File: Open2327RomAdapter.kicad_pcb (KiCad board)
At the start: 2 copper layers, 19.6 x 40.6 mm, 5 parts, among them P1 CONN_01X02, U1 2364, U2 27128

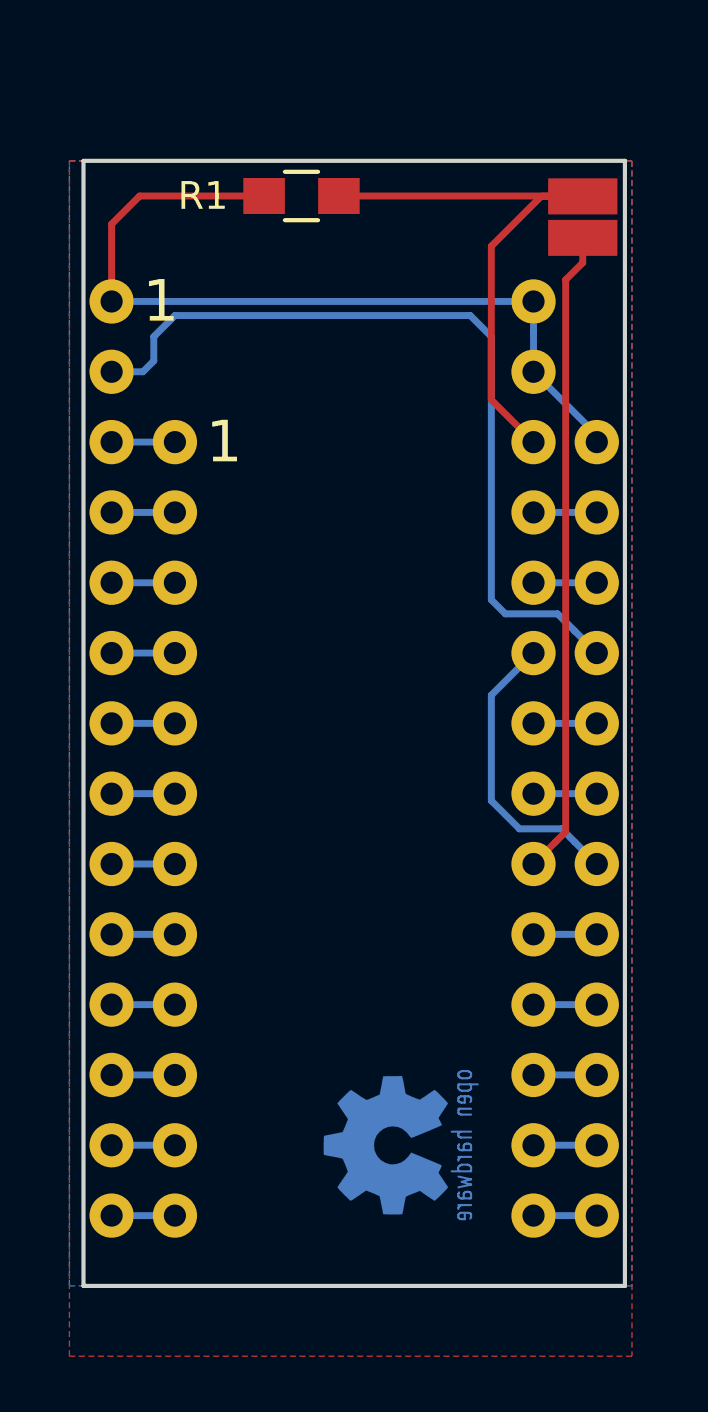
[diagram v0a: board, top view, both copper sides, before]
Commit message: Add pull-up resistors
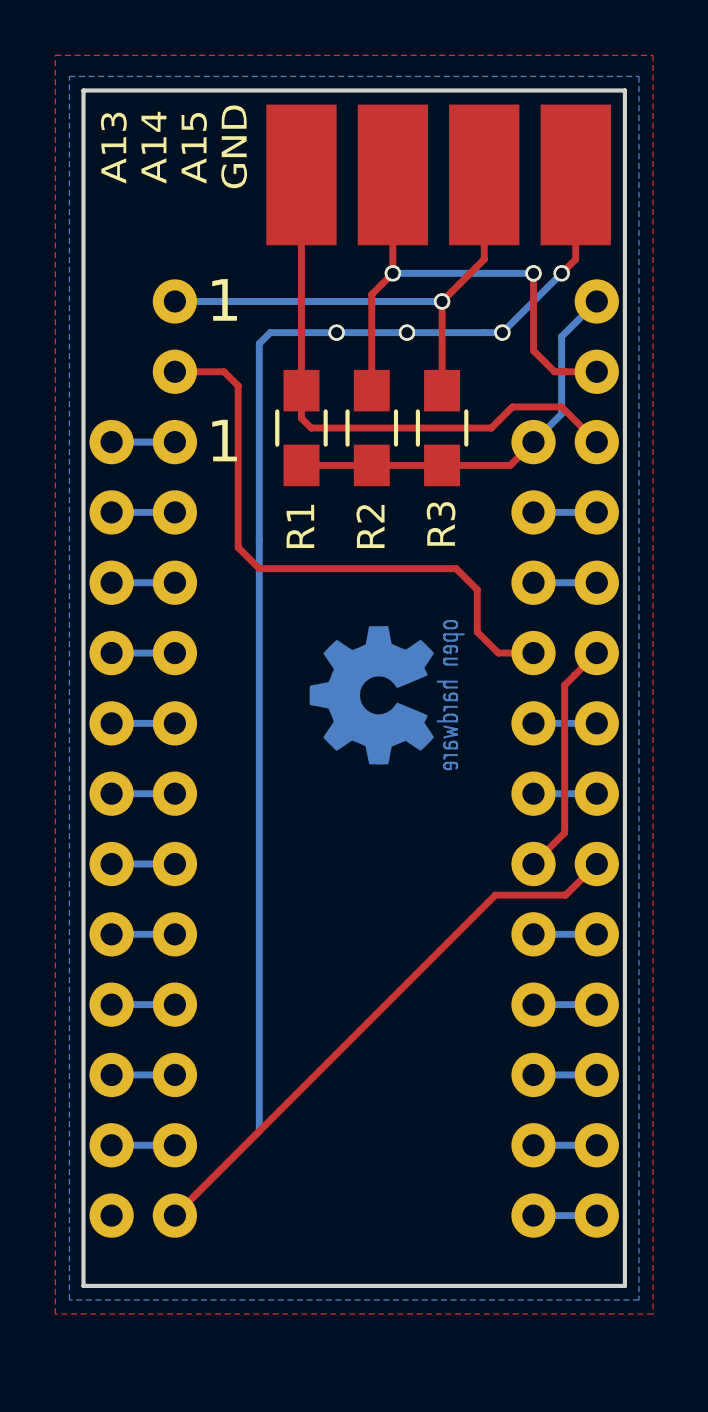
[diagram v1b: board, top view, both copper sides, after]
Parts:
- added R2: 10K, Resistors_SMD:R_0805_HandSoldering, F.Cu at (155.7, 106.2)
- added R3: 10K, Resistors_SMD:R_0805_HandSoldering, F.Cu at (158.2, 106.2)
- P1: value CONN_01X02 -> CONN_01X04; footprint Sukko:LoosePads-2-NoSilkS -> Sukko:LoosePads-4
- moved G*** 16.3 mm to (155.7, 115.8)
- moved R1 8.38 mm to (153.2, 106.2), turned to 270 degrees
- moved P1 5.55 mm to (158.0, 97.0)
- moved U1 2.29 mm to (146.3, 106.7)
- moved U2 2.29 mm to (148.6, 101.6)
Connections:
- R1 pad 1: Net-(P1-Pad2) -> Net-(P1-Pad4)
- U2 pad 1: VCC -> Net-(P1-Pad2)
- U2 pad 26: Net-(P1-Pad2) -> Net-(P1-Pad4)
- U2 pad 27: VCC -> Net-(P1-Pad3)
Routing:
- net GND: track 25.6 -> 69.0 mm, vias 0 -> 4
- net Net-(P1-Pad4): track 0.00 -> 20.4 mm
- net Net-(P1-Pad3): track 0.00 -> 18.6 mm, vias 0 -> 2
- net VCC: track 30.2 -> 14.8 mm
- net Net-(U1-Pad21): track 29.5 -> 21.5 mm
- net Net-(P1-Pad2): track 20.6 -> 18.1 mm, vias 0 -> 1
- net Net-(U1-Pad18): track 10.7 -> 8.57 mm
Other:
- board size 19.6 x 40.6 mm -> 19.6 x 43.2 mm
- board text added: "A13 A14 A15 GND"
- board text added: "https://github.com/SukkoPera/Open2327RomAdapter"
- board text removed: "https://github.com/SukkoPera/"

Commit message: Move pull-up resistors to bottom of board
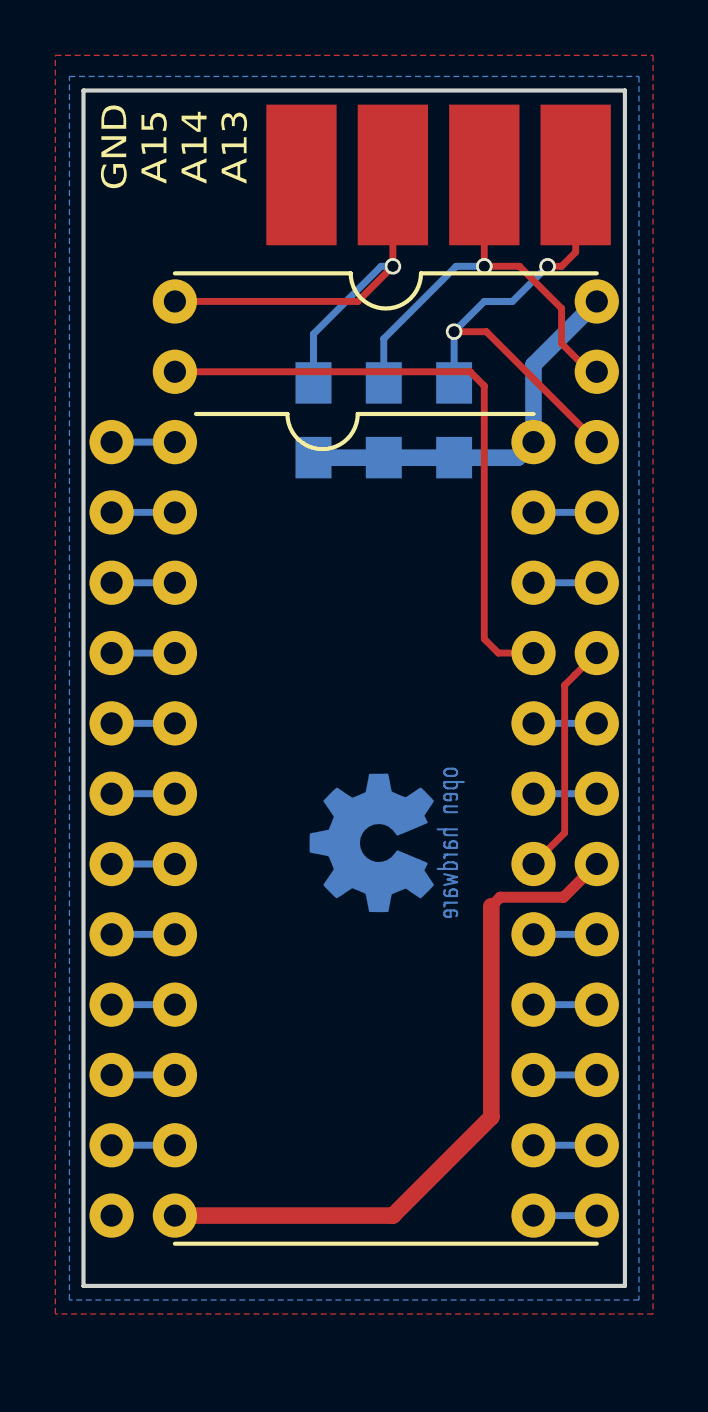
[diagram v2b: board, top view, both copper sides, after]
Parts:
- R1, R2, R3: moved to B.Cu
- U1: footprint Sukko:DIP-24_W15.24mm-NoSilkS -> Sukko:DIP-24_W15.24mm-Notch
- U2: footprint Sukko:DIP-28_W15.24mm-NoSilkS -> Sukko:DIP-28_W15.24mm-Notch
- moved R1 5.52 mm to (158.7, 105.9)
- moved G*** 5.33 mm to (155.7, 121.2)
- moved R3 4.66 mm to (153.6, 105.9)
- moved R2 0.52 mm to (156.1, 105.9)
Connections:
- P1 pad 1: GND -> Net-(P1-Pad1)
- P1 pad 4: Net-(P1-Pad4) -> GND
- R1 pad 1: Net-(P1-Pad4) -> Net-(P1-Pad1)
- R2 pad 1: Net-(P1-Pad3) -> Net-(P1-Pad2)
- R3 pad 1: Net-(P1-Pad2) -> Net-(P1-Pad3)
- U2 pad 1: Net-(P1-Pad2) -> Net-(P1-Pad3)
- U2 pad 26: Net-(P1-Pad4) -> Net-(P1-Pad1)
- U2 pad 27: Net-(P1-Pad3) -> Net-(P1-Pad2)
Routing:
- net GND: track 69.0 -> 25.0 mm, vias 4 -> 0
- net Net-(P1-Pad4): track 20.4 -> 0.00 mm
- net Net-(P1-Pad1): track 0.00 -> 17.0 mm, vias 0 -> 2
- net Net-(P1-Pad2): track 18.1 -> 16.0 mm
- net Net-(P1-Pad3): track 18.6 -> 17.4 mm, vias 2 -> 1
- net Net-(U1-Pad21): track 21.5 -> 22.5 mm
- net VCC: track 14.8 -> 14.2 mm
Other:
- net class Power added: clearance 0.2, trace_width 0.6, via_dia 0.8, via_drill 0.6
- board text added: "GND A15 A14 A13"
- board text removed: "1"
- board text removed: "A13 A14 A15 GND"

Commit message: Update board This should be the board that went to prototype production. It has been tested and is working great!
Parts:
- U1: footprint Sukko:DIP-24_W15.24mm-Notch -> Open2327RomAdapter:DIP-24_W15.24mm-Notch
- U2: footprint Sukko:DIP-28_W15.24mm-Notch -> Open2327RomAdapter:DIP-28_W15.24mm-Notch
- turned P1 to 0 degrees
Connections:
- P1 pad 1: Net-(P1-Pad1) -> GND
- P1 pad 4: GND -> Net-(P1-Pad4)
- R1 pad 1: Net-(P1-Pad1) -> Net-(P1-Pad4)
- R2 pad 1: Net-(P1-Pad2) -> Net-(P1-Pad3)
- R3 pad 1: Net-(P1-Pad3) -> Net-(P1-Pad2)
- U2 pad 1: Net-(P1-Pad3) -> Net-(P1-Pad2)
- U2 pad 26: Net-(P1-Pad1) -> Net-(P1-Pad4)
- U2 pad 27: Net-(P1-Pad2) -> Net-(P1-Pad3)
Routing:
- net Net-(P1-Pad4): track 0.00 -> 17.0 mm, vias 0 -> 2
- net Net-(P1-Pad1): track 17.0 -> 0.00 mm, vias 2 -> 0
- net Net-(P1-Pad3): track 17.4 -> 16.0 mm
- net Net-(P1-Pad2): track 16.0 -> 17.4 mm

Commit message: Cleanup
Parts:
- P1: footprint Sukko:LoosePads-4 -> Open2327RomAdapter:LoosePads-4
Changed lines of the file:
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@@
     )
-  )
-  (module Sukko:LoosePads-4 (layer F.Cu)
-    (at 157.988 97.028)
-    (fp_text reference P1 (at 0 3.556) (layer F.SilkS) hide
-      (effects (font (size 1 1) (thickness 0.15)))
-    )
-    (fp_text value CONN_01X04 (at 0 -3.556) (layer F.Fab) hide
-      (effects (font (size 1 1) (thickness 0.15)))
-    )
-    (pad 1 smd rect (at -5.08 0 90) (size 5.08 2.54) (layers F.Cu F.Paste F.Mask)
-      (net 1 GND))
-    (pad 2 smd rect (at -1.778 0 90) (size 5.08 2.54) (layers F.Cu F.Paste F.Mask)
-      (net 25 "Net-(P1-Pad2)"))
-    (pad 3 smd rect (at 1.524 0 90) (size 5.08 2.54) (layers F.Cu F.Paste F.Mask)
-      (net 26 "Net-(P1-Pad3)"))
-    (pad 4 smd rect (at 4.826 0 90) (size 5.08 2.54) (layers F.Cu F.Paste F.Mask)
-      (net 27 "Net-(P1-Pad4)"))
   )
   (module Resistors_SMD:R_0805_HandSoldering (layer B.Cu)
@@
     )
   )
+  (module Open2327RomAdapter:LoosePads-4 (layer F.Cu)
+    (at 157.988 97.028)
+    (fp_text reference P1 (at 0 3.556) (layer F.SilkS)
+      (effects (font (size 1 1) (thickness 0.15)))
+    )
+    (fp_text value CONN_01X04 (at 0 -3.556) (layer F.Fab) hide
+      (effects (font (size 1 1) (thickness 0.15)))
+    )
+    (pad 1 smd rect (at -5.08 0 90) (size 5.08 2.54) (layers F.Cu F.Paste F.Mask)
+      (net 1 GND))
+    (pad 2 smd rect (at -1.778 0 90) (size 5.08 2.54) (layers F.Cu F.Paste F.Mask)
+      (net 25 "Net-(P1-Pad2)"))
+    (pad 3 smd rect (at 1.524 0 90) (size 5.08 2.54) (layers F.Cu F.Paste F.Mask)
+      (net 26 "Net-(P1-Pad3)"))
+    (pad 4 smd rect (at 4.826 0 90) (size 5.08 2.54) (layers F.Cu F.Paste F.Mask)
+      (net 27 "Net-(P1-Pad4)"))
+  )
   (gr_text "GND\nA15\nA14\nA13" (at 148.59 96.012 90) (layer F.SilkS)
